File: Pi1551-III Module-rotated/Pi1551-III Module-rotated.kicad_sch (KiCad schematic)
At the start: 30 parts, among them J1 DC IN, J3 TCBM, J4 Mini-DIN-7, J8 Module_Panel, M1 Mounting, M2 Mounting, M3 Mounting, M4 Mounting, Q1 MMBT3904, Q2 MMBT3904, Q3 MMBT3904, Q4 MMBT3904

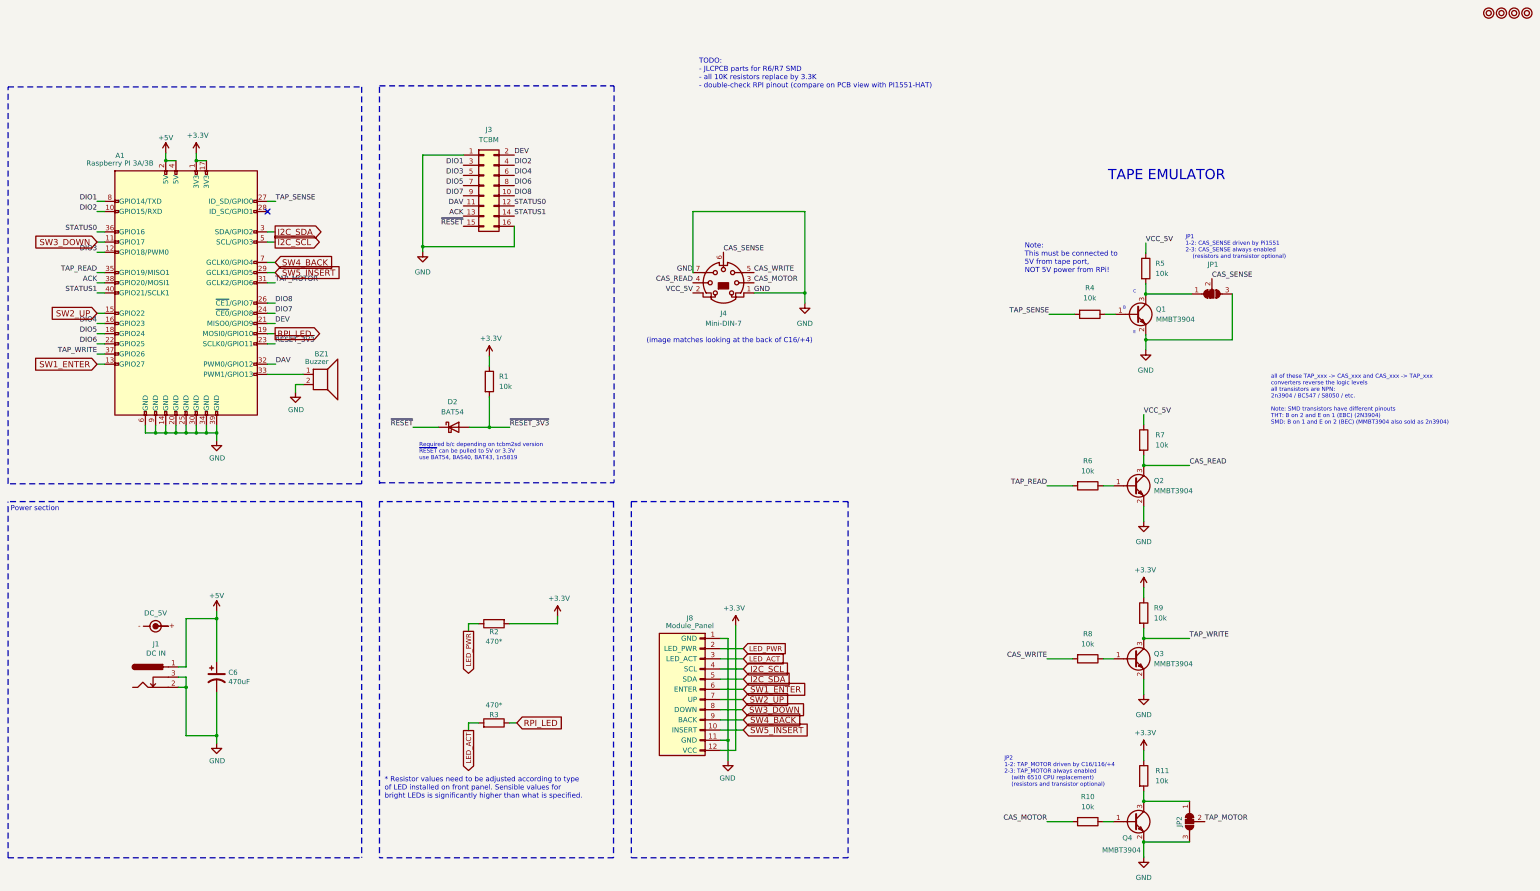
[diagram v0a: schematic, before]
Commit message: all 10K resistors to 3.3K, JLPCB part numbers for 470R resistors, 1.2mm track width for 5V - as short as possible
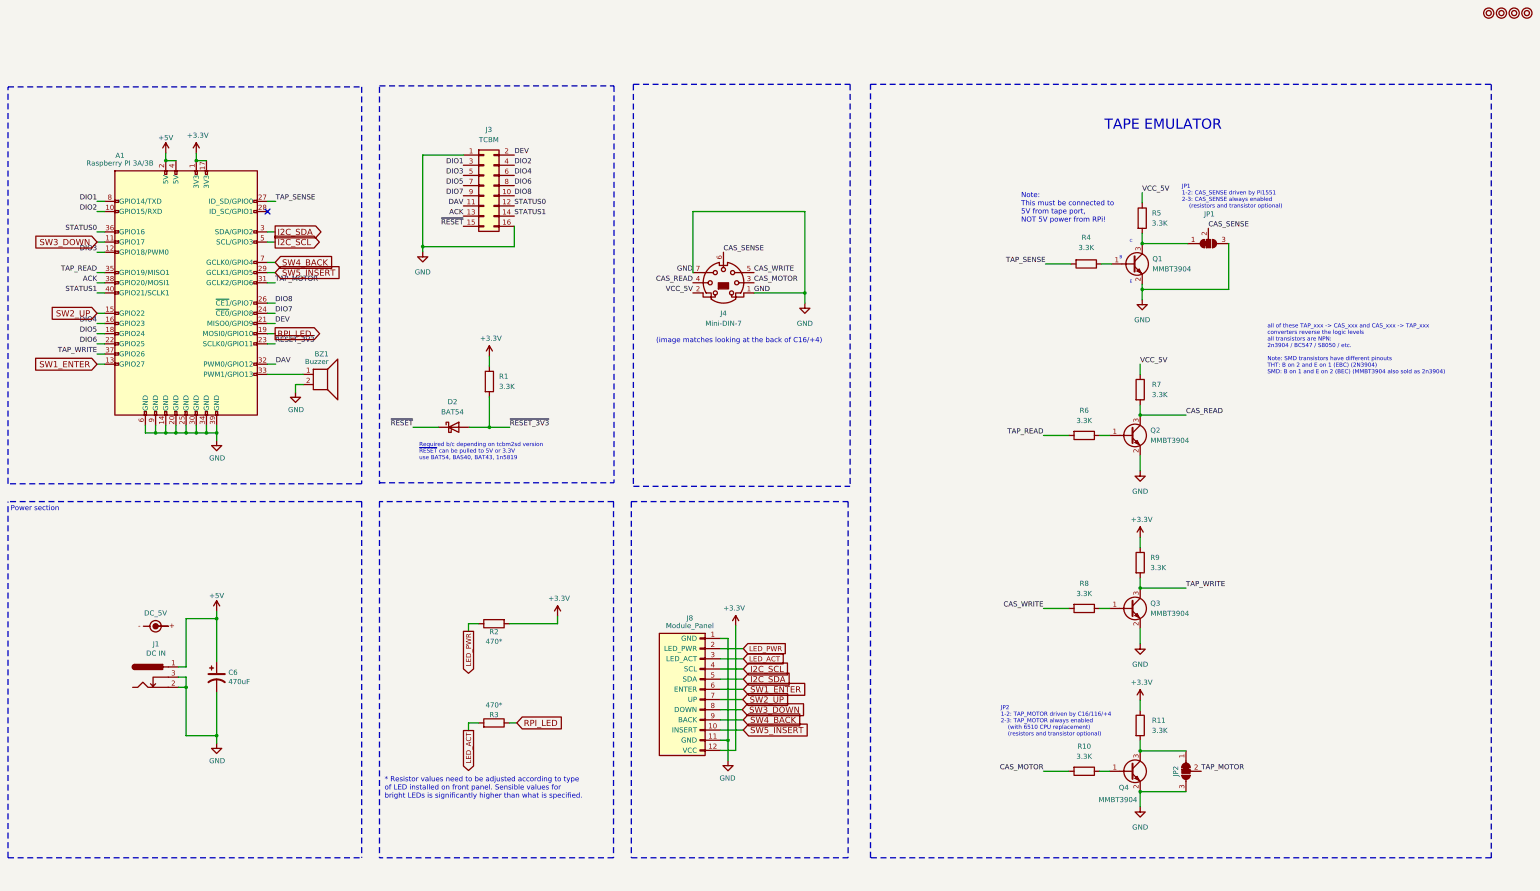
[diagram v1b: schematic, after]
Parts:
- R1, R10, R11, R4, R5, R6, R7, R8, R9: value 10k -> 3.3K; JLCPCB Part # C22356686 -> C26010; JLCPCB URL https://jlcpcb.com/partdetail/23790130-RCA0510KFLF/C22356686 -> https://jlcpcb.com/partdetail/26753-0805W8F3301T5E/C26010; MFR.Part # RCA0510KFLF -> 0805W8F3301T5E
- R2, R3: JLCPCB Part # (none) -> C17710; JLCPCB URL (none) -> https://jlcpcb.com/partdetail/18398-0805W8F4700T5E/C17710; MFR.Part # (none) -> 0805W8F4700T5E
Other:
- note removed: "TODO: - JLCPCB parts for R6/R7 SMD - all 10K resistors replace by 3.3K - double-check RPI pinout (compare on PCB view with PI1551-HAT)"
- title: PI1541-III Module -> PI1541-III Module (rotated)
- moved on the sheet: JP1, JP2, Q1, Q2, Q3, Q4, R10, R11, R4, R5, R6, R7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

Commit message: gerber files for fabrication
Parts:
- M1, M2, M3, M4: now left out of the parts list
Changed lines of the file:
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@@
 		(unit 1)
 		(exclude_from_sim no)
-		(in_bom yes)
+		(in_bom no)
 		(on_board yes)
 		(dnp no)
@@
 		(unit 1)
 		(exclude_from_sim no)
-		(in_bom yes)
+		(in_bom no)
 		(on_board yes)
 		(dnp no)
@@
 		(unit 1)
 		(exclude_from_sim no)
-		(in_bom yes)
+		(in_bom no)
 		(on_board yes)
 		(dnp no)
@@
 		(unit 1)
 		(exclude_from_sim no)
-		(in_bom yes)
-		(on_board yes)
-		(dnp no)
+		(in_bom no)
+		(on_board yes)
+		(dnp no)

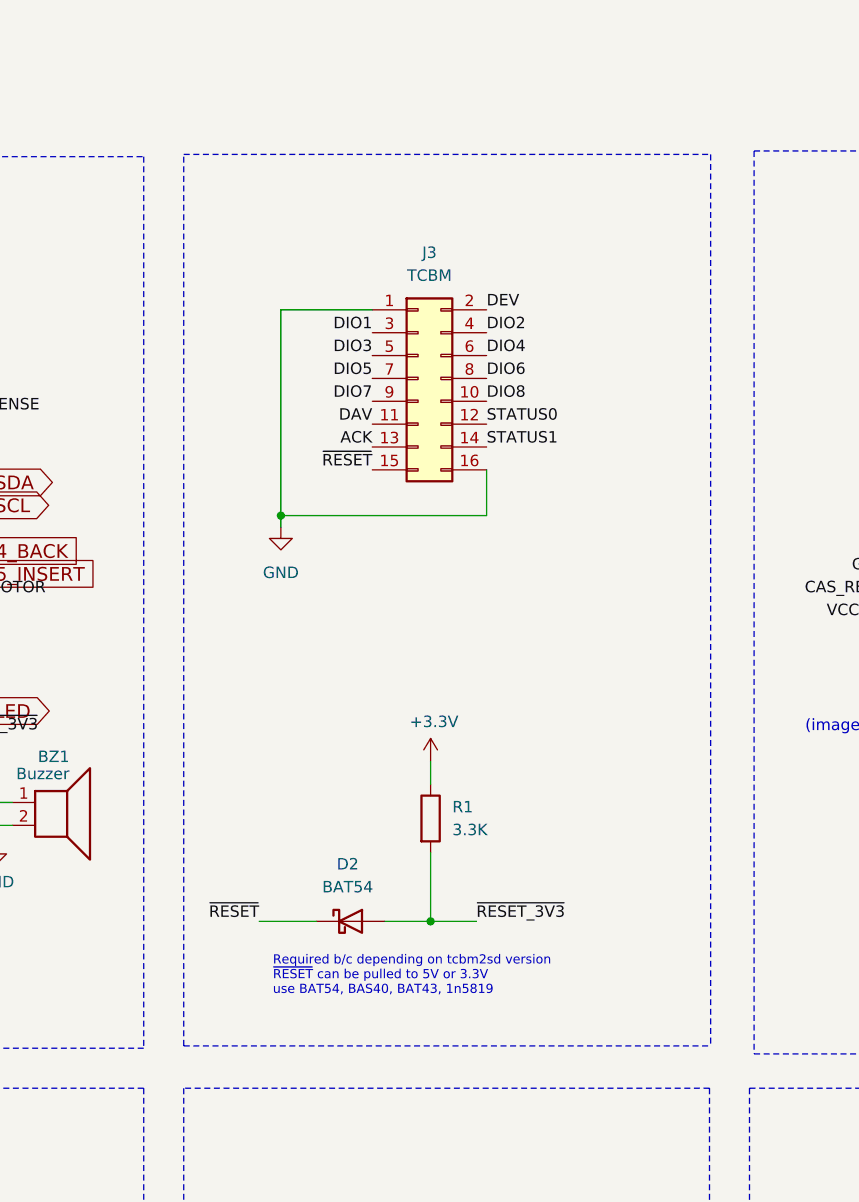
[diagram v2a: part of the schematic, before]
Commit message: revision 2 - pullups on all TCBM lines
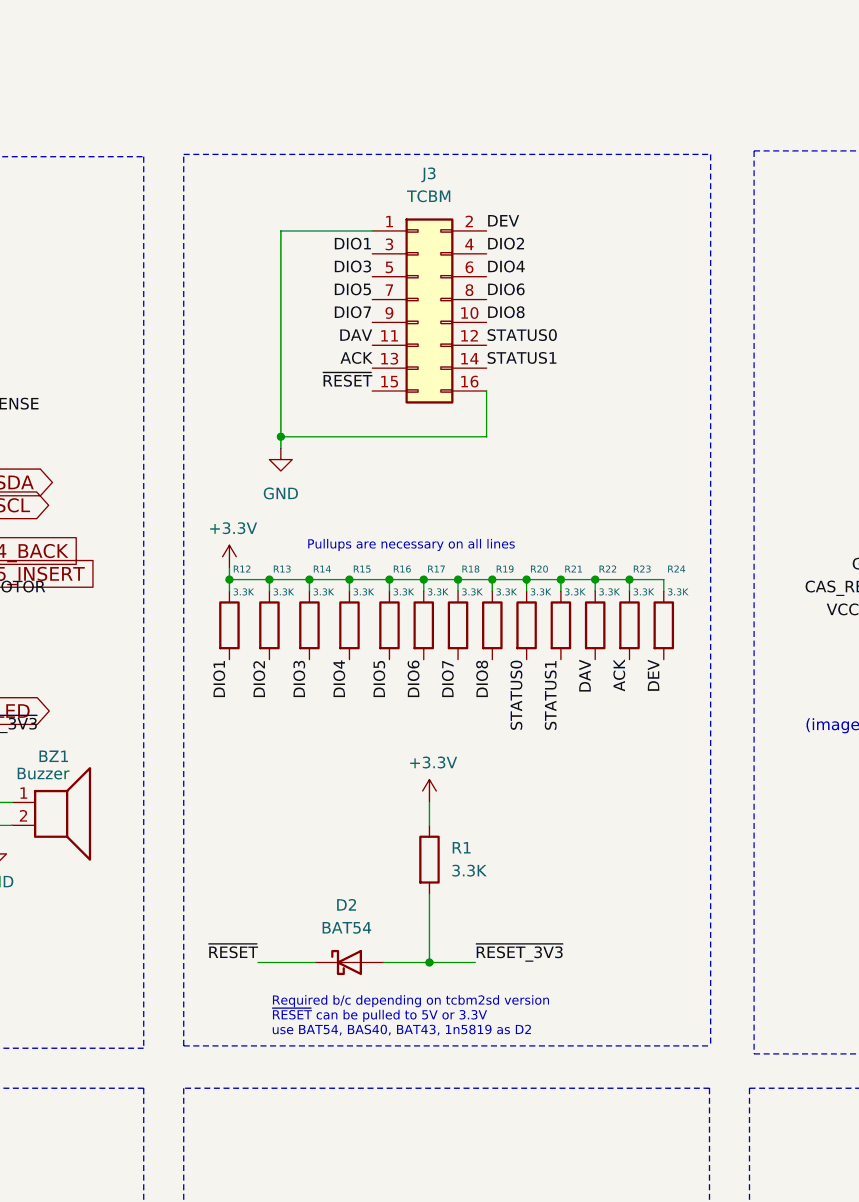
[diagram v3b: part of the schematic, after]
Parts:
- added R12, R13, R14, R15, R16, R17, R18, R19, R20, R21, R22, R23, R24: 3.3K, Resistor_SMD:R_0805_2012Metric_Pad1.20x1.40mm_HandSolder, symbol Device:R
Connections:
- net +3.3V: now also R12.1, R13.1, R14.1, R15.1, R16.1, R17.1, R18.1, R19.1, R20.1, R21.1, R22.1, R23.1, R24.1
- net ACK: now also R23.2
- net DAV: now also R22.2
- net DEV: now also R24.2
- net DIO1: now also R12.2
- net DIO2: now also R13.2
- net DIO3: now also R14.2
- net DIO4: now also R15.2
- net DIO5: now also R16.2
- net DIO6: now also R17.2
- net DIO7: now also R18.2
- net DIO8: now also R19.2
- net STATUS0: now also R20.2
- net STATUS1: now also R21.2
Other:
- note added: "Pullups are necessary on all lines"
- note added: "Required b/c depending on tcbm2sd version ~{RESET} can be pulled to 5V or 3.3V use BAT54, BAS40, BAT43, 1n5819 as D2"
- note removed: "Required b/c depending on tcbm2sd version ~{RESET} can be pulled to 5V or 3.3V use BAT54, BAS40, BAT43, 1n5819"
- moved on the sheet: D2, J3, R1
